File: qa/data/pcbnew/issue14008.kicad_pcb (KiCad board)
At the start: 2 copper layers, 72 x 52 mm, 5 parts, among them Q1 DMP3098L-7-ALPHA

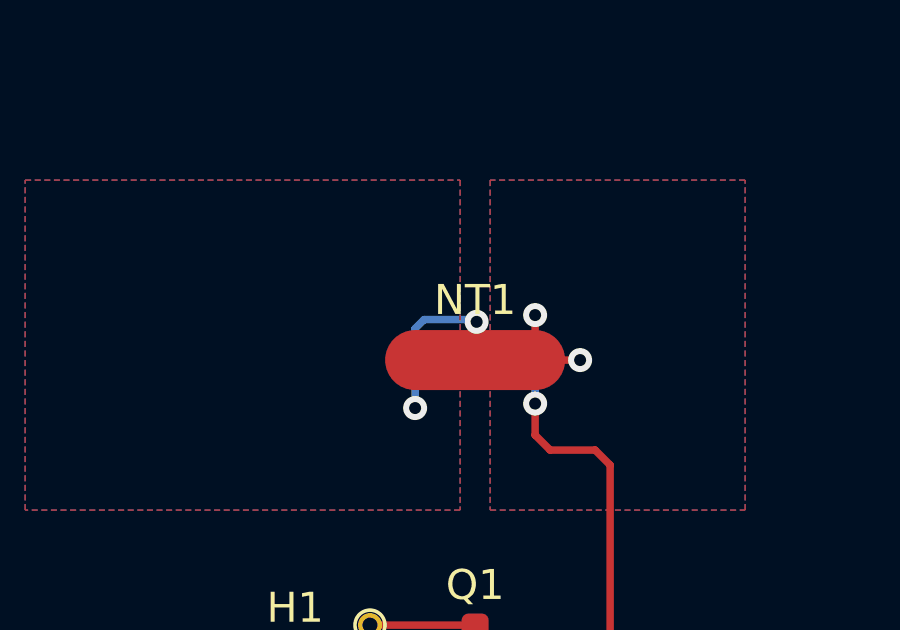
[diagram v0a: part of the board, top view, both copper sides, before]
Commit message: Hand cherry-pick hole clearance fixes for #21941.
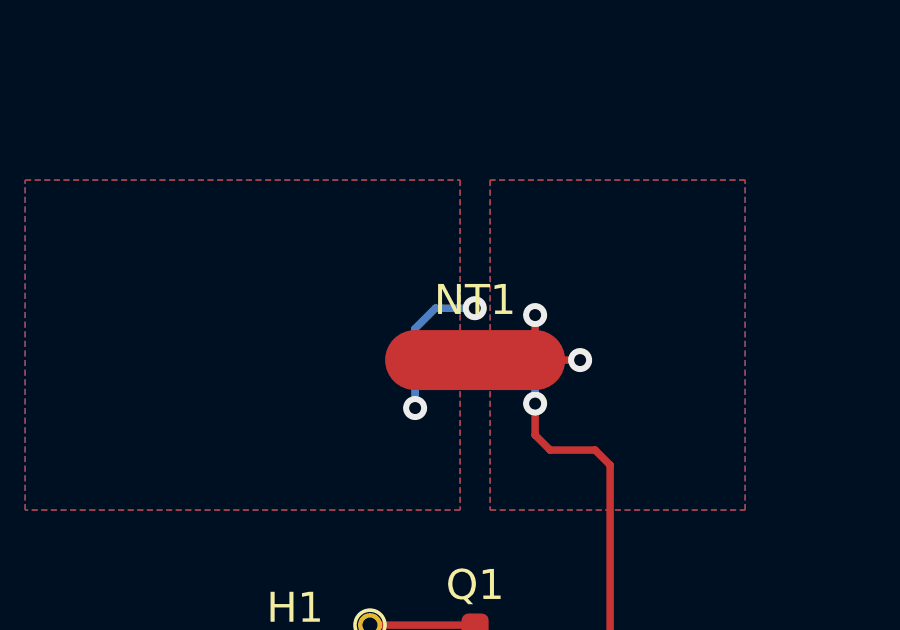
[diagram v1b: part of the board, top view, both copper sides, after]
